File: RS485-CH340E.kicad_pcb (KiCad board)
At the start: 2 copper layers, 24.1 x 14.5 mm, 14 parts, among them J1 USB_A, J2 Conn_01x04_Pin, J3 Conn_02x04_Odd_Even, U1 NCP1117-3.3_SOT223, U2 SP3485CN, U3 CH340X

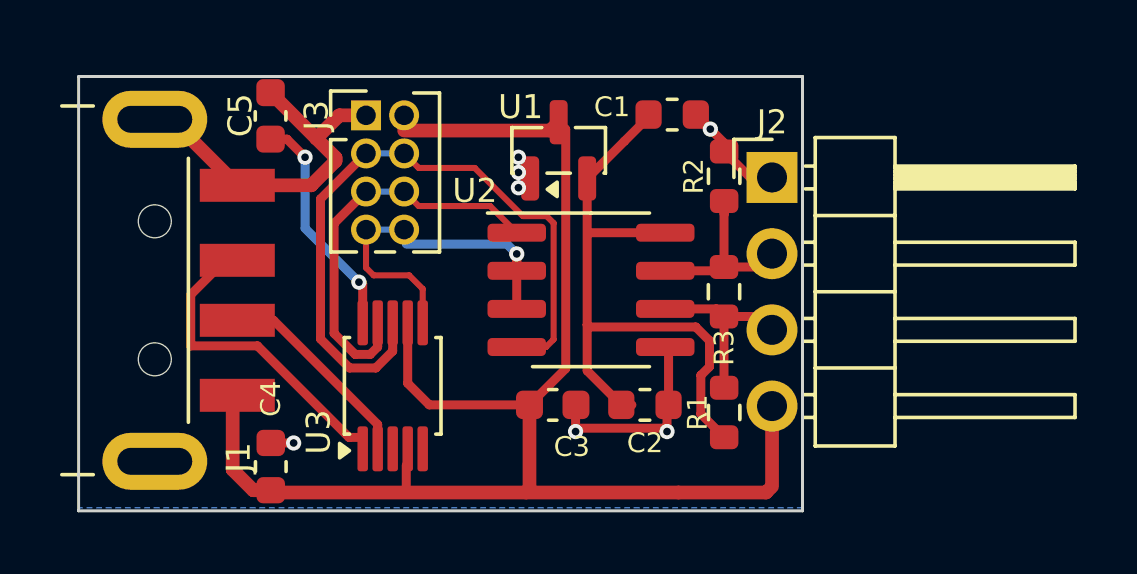
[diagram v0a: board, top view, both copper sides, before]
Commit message: Remove 3.3V LDO voltage regulator (use ch340 built-in LDO) Run rs485 transceiver at 5V Make design easier to hand solder
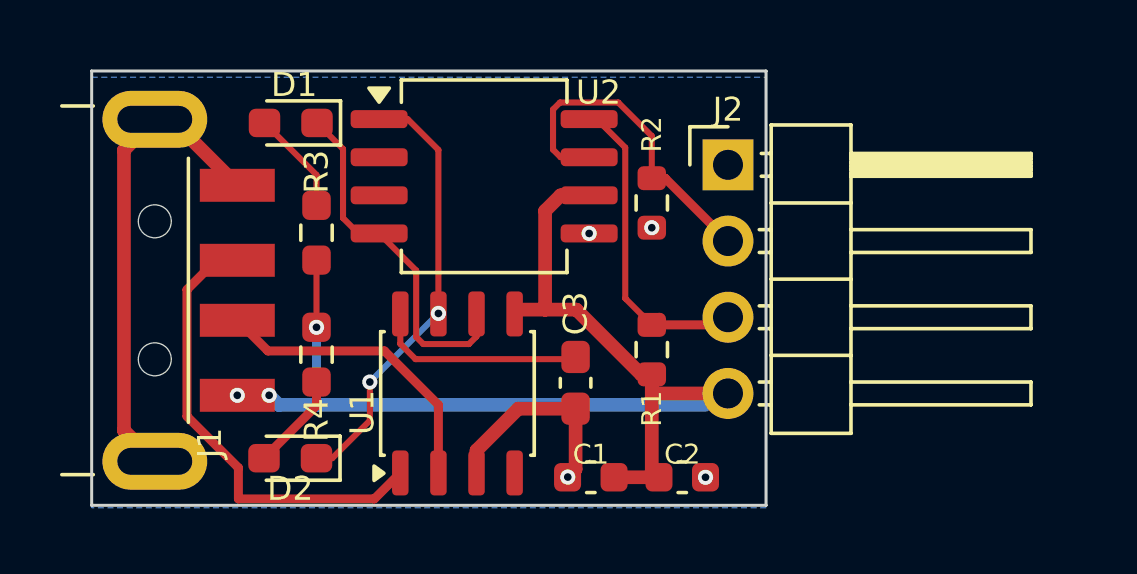
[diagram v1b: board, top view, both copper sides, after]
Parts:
- removed C4: 1uF, Capacitor_SMD:C_0603_1608Metric
- removed C5: 100nF, Capacitor_SMD:C_0603_1608Metric
- removed J3: Conn_02x04_Odd_Even, Connector_PinHeader_1.27mm:PinHeader_2x04_P1.27mm_Vertical
- removed the U1 at (145.0, 89.1)
- added D1: LED, LED_SMD:LED_0603_1608Metric_Pad1.05x0.95mm_HandSolder, F.Cu at (136.0, 88.1)
- added D2: LED, LED_SMD:LED_0603_1608Metric_Pad1.05x0.95mm_HandSolder, F.Cu at (136.0, 99.3)
- added R4: 470, Resistor_SMD:R_0603_1608Metric_Pad0.98x0.95mm_HandSolder, F.Cu at (136.9, 95.9)
- C1: value 100nF -> 1uF
- C2: value 1uF -> 100nF
- C3: footprint Capacitor_SMD:C_0603_1608Metric -> Capacitor_SMD:C_0603_1608Metric_Pad1.08x0.95mm_HandSolder
- R1, R2: value 20K -> 4.7K
- R3: value 120 -> 470; footprint Resistor_SMD:R_0603_1608Metric -> Resistor_SMD:R_0603_1608Metric_Pad0.98x0.95mm_HandSolder
- U1: renamed from U3; value CH340X -> CH340N; footprint Package_SO:MSOP-10_3x3mm_P0.5mm -> Package_SO:JEITA_SOIC-8_3.9x4.9mm_P1.27mm
- U2: value SP3485CN -> THVD1406DR; footprint Package_SO:SOIC-8_3.9x4.9mm_P1.27mm -> Package_SO:SOIC-8_5.3x6.2mm_P1.27mm
- moved R3 13.7 mm to (136.9, 91.8)
- moved C1 12.4 mm to (146.1, 99.9), turned to 180 degrees
- moved U2 5.20 mm to (142.5, 89.9)
- moved R1 3.20 mm to (148.1, 95.7)
- moved C2 2.72 mm to (149.1, 99.9)
- moved R2 2.57 mm to (148.1, 90.8), turned to -90 degrees
- moved U1 2.17 mm to (141.6, 97.2)
- moved J2 1.53 mm to (150.6, 89.5)
- moved C3 1.06 mm to (145.5, 96.8), turned to -90 degrees
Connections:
- C1 pad 1: +3.3V -> +5V
- C2 pad 1: +3.3V -> +5V
- C3 pad 1: VCC -> Net-(U1-V3)
- J1 pad 1: VCC -> +5V
- J2 pad 4: VCC -> +5V
- R1 pad 1: +3.3V -> +5V
- R3 pad 1: /A -> +5V
- R3 pad 2: /B -> Net-(D1-A)
- U1 pad 5: unconnected-(U3-~{CTS}-Pad5) -> +5V
- U1 pad 6: /TXE -> /TxD
- U1 pad 7: VCC -> /RxD
- U1 pad 8: /TxD -> Net-(U1-V3)
- U2 pad 2: /TXE -> unconnected-(U2-*RE-Pad2)
- U2 pad 3: /TXE -> unconnected-(U2-*SHDN-Pad3)
- U2 pad 6: /A -> +5V
- U2 pad 8: +3.3V -> /A
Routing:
- net VCC: track 49.6 -> 0.00 mm
- net +5V: track 0.00 -> 38.4 mm, vias 0 -> 3
- net +3.3V: track 21.5 -> 0.00 mm
- net /TXE: track 12.1 -> 0.00 mm, vias 1 -> 0
- net /TxD: track 23.2 -> 11.9 mm
- net Net-(U3-V3): track 7.38 -> 0.00 mm, vias 2 -> 0
- net Net-(U1-V3): track 0.00 -> 7.08 mm
- net /B: track 6.44 -> 11.9 mm
- net Net-(J1-D+): track 10.7 -> 15.5 mm
- net /A: track 6.23 -> 10.6 mm
- net Net-(J1-D-): track 6.55 -> 10.1 mm
- net Net-(D1-A): track 0.00 -> 3.46 mm
- net Net-(D2-A): track 0.00 -> 3.26 mm
- net /RxD: track 13.4 -> 14.7 mm, vias 0 -> 2
- net GND: track 23.7 -> 22.9 mm, vias 7 -> 4
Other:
- board size 24.1 x 14.5 mm -> 22.5 x 14.5 mm
- board text added: "+5V"
- board text removed: "VCC"
